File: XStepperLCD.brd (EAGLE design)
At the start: 12.4 x 41.9 mm, 7 parts, among them U1 Attiny85

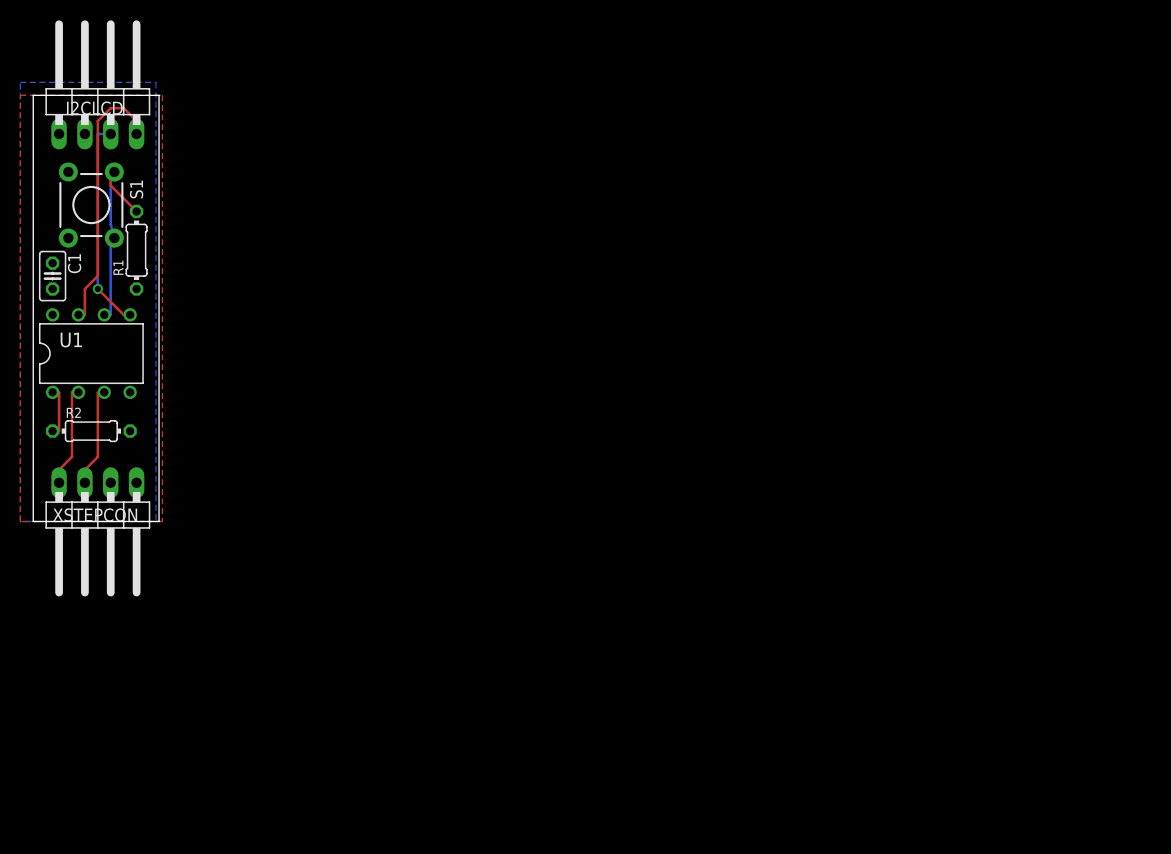
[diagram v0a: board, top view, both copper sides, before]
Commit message: First konzept for XLCD with 328p
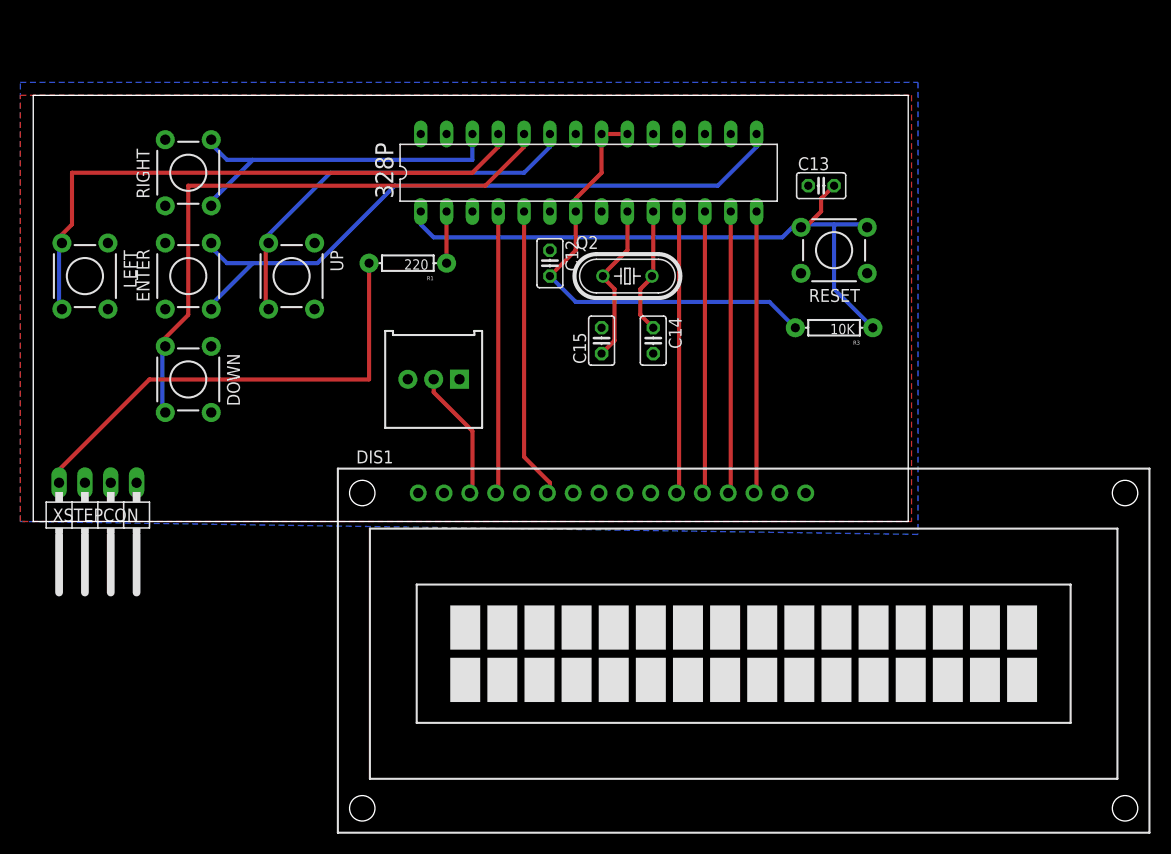
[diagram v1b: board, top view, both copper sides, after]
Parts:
- removed C1: 100nF, rcl:C025-025X050
- removed I2CLCD: i2c, pinhead:1X04/90
- removed S1: Control, SparkFun-Electromechanical:TACTILE-PTH
- removed U1: Attiny85, _hhn_attiny25_45_85:PDIP08_300MIL
- added 328P: CONTROLLER, Bibsatmel:DIL28-3
- added C12, C13: 0.1uF, resistor:C025-025X050
- added C14, C15: 18pF, resistor:C025-025X050
- added DIS1: TUXGR_16X2_R2, display-lcd:TUXGR_16X2_R2
- added DOWN, ENTER, LEFT, RIGHT, UP: (no value), SparkFun:TACTILE-PTH
- added Q2: 16 MHZ, crystal:HC49/S
- added R3: 10K, SparkFun-Resistors:AXIAL-0.3
- added RESET: RESET, SparkFun:TACTILE-PTH
- R1: value 10k -> 220; device resistor:0204/7 -> SparkFun-Resistors:AXIAL-0.3
- R2: value 10k -> 10K; device resistor:0204/7 -> SparkFun-Electromechanical:3386U
- moved R2 34.0 mm to (39.4, 14.0), turned to 180 degrees
- moved R1 26.7 mm to (36.8, 25.4), turned to 180 degrees
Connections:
- removed net CTRL: R1.2, S1.1, S1.2, U1.6
- removed net SCL: I2CLCD.4, U1.7
- removed net SDA: I2CLCD.3, U1.5
- new net 5V: 328P.20, 328P.21, 328P.7, C12.2, R3.P$2
- new net D4: 328P.11, DIS1.11
- new net D5: 328P.12, DIS1.12
- new net D6: 328P.13, DIS1.13
- new net D7: 328P.14, DIS1.14
- new net DOWN: 328P.24, DOWN.3, DOWN.4
- new net E: 328P.5, DIS1.6
- new net ENTER: 328P.15, ENTER.3, ENTER.4
- new net LEFT: 328P.25, LEFT.3, LEFT.4
- new net N$2: DIS1.3, R2.2
- new net N$33: 328P.9, C15.1, Q2.1
- new net N$34: 328P.10, C14.1, Q2.2
- new net RESET: 328P.1, C13.2, R3.P$1, RESET.3, RESET.4
- new net RIGHT: 328P.26, RIGHT.3, RIGHT.4
- new net RS: 328P.4, DIS1.4
- new net TXD: 328P.3
- new net UP: 328P.23, UP.3, UP.4
- net GND: now also 328P.22, 328P.8, C12.1, C13.1, C14.2, C15.2, DIS1.1, DIS1.5, DOWN.1, DOWN.2, ENTER.1, ENTER.2, LEFT.1, LEFT.2, R2.3, RESET.1, RESET.2, RIGHT.1, RIGHT.2, UP.1, UP.2; no longer C1.2, I2CLCD.1, R1.1, U1.4
- net N$1: now also 328P.2, R1.P$1; no longer R2.1, U1.1
- net RX: now also R1.P$2; no longer U1.2
- net TX: no longer U1.3
- net VCC: now also DIS1.2, R2.1; no longer C1.1, I2CLCD.2, R2.2, S1.3, S1.4, U1.8
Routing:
- net ENTER: track 0.00 -> 66.8 mm
- net RESET: track 0.00 -> 63.7 mm
- net DOWN: track 0.00 -> 59.4 mm
- net LEFT: track 0.00 -> 58.3 mm
- net 5V: track 0.00 -> 44.8 mm
- net UP: track 0.00 -> 40.1 mm
- net RX: track 10.1 -> 46.9 mm
- net RIGHT: track 0.00 -> 35.4 mm
- net E: track 0.00 -> 29.4 mm
- net RS: track 0.00 -> 28.3 mm
- net D7: track 0.00 -> 28.3 mm
- net D6: track 0.00 -> 28.3 mm
- net D5: track 0.00 -> 28.3 mm
- net D4: track 0.00 -> 28.3 mm
- net SCL: track 26.3 -> 0.00 mm
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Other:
- board size 12.4 x 41.9 mm -> 86 x 41.9 mm

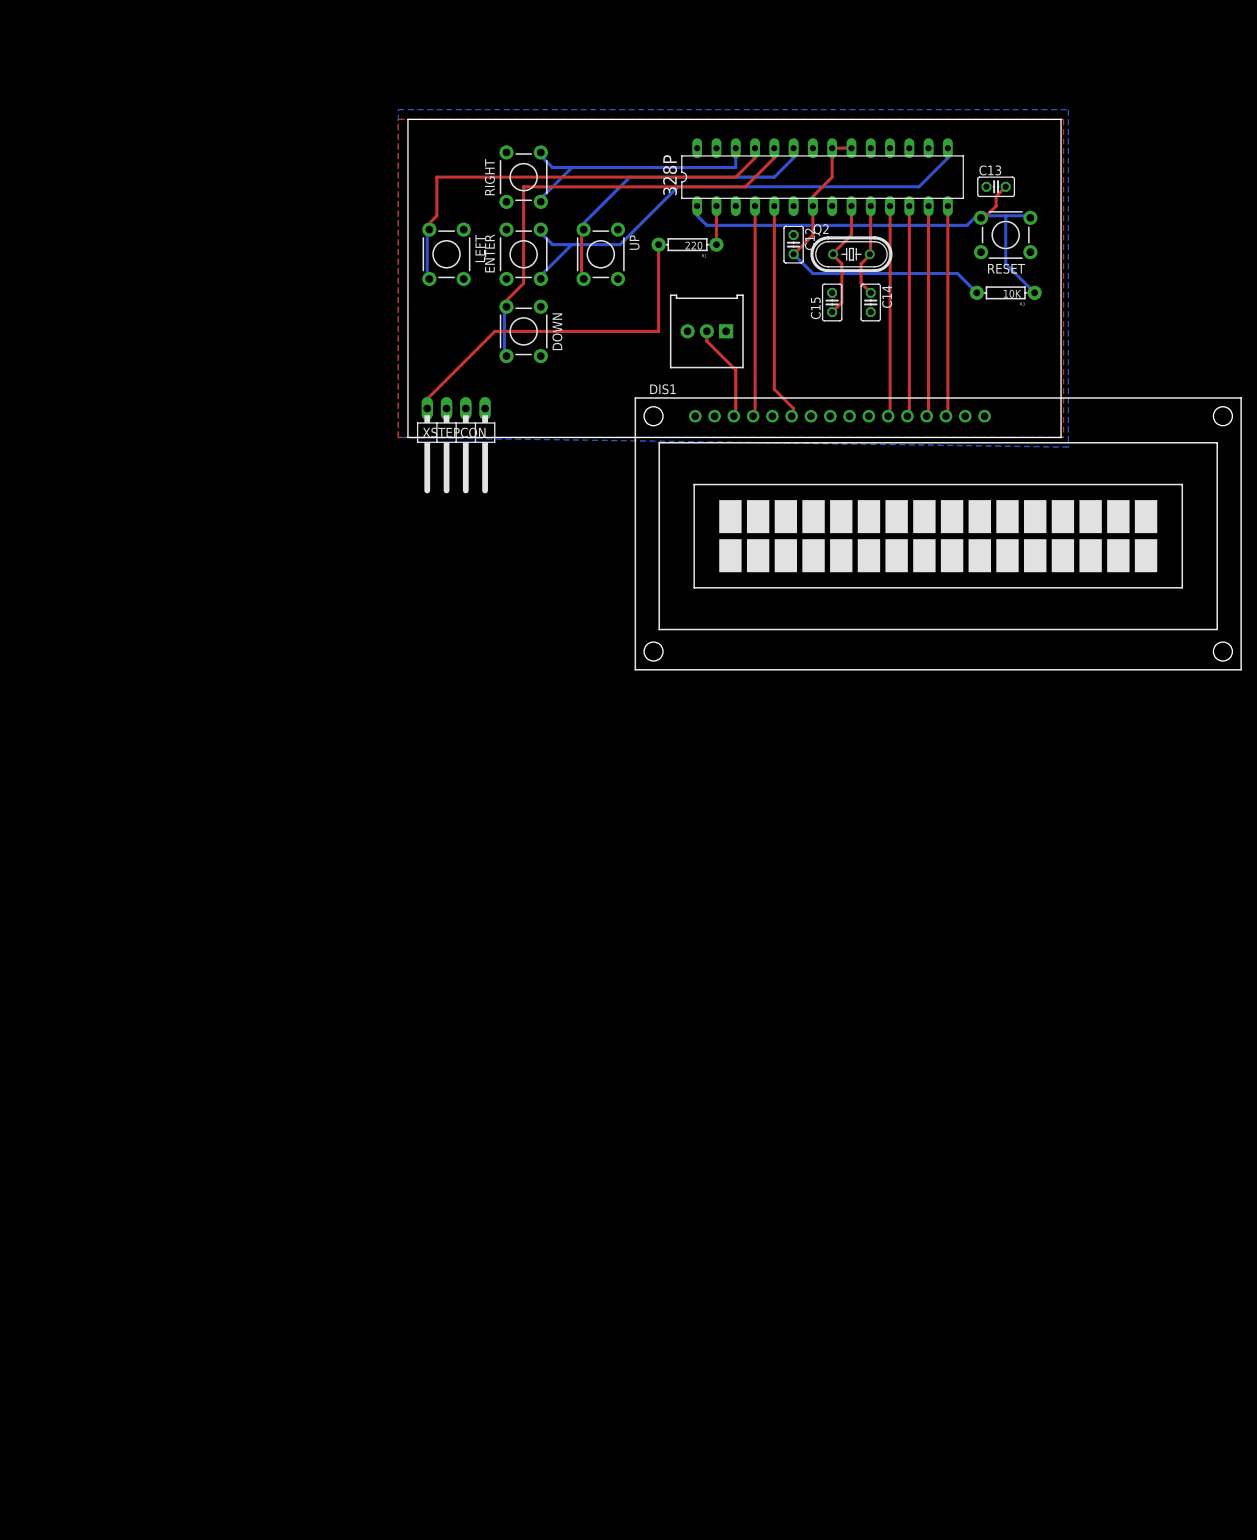
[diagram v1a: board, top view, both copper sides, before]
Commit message: add conn header for buttons
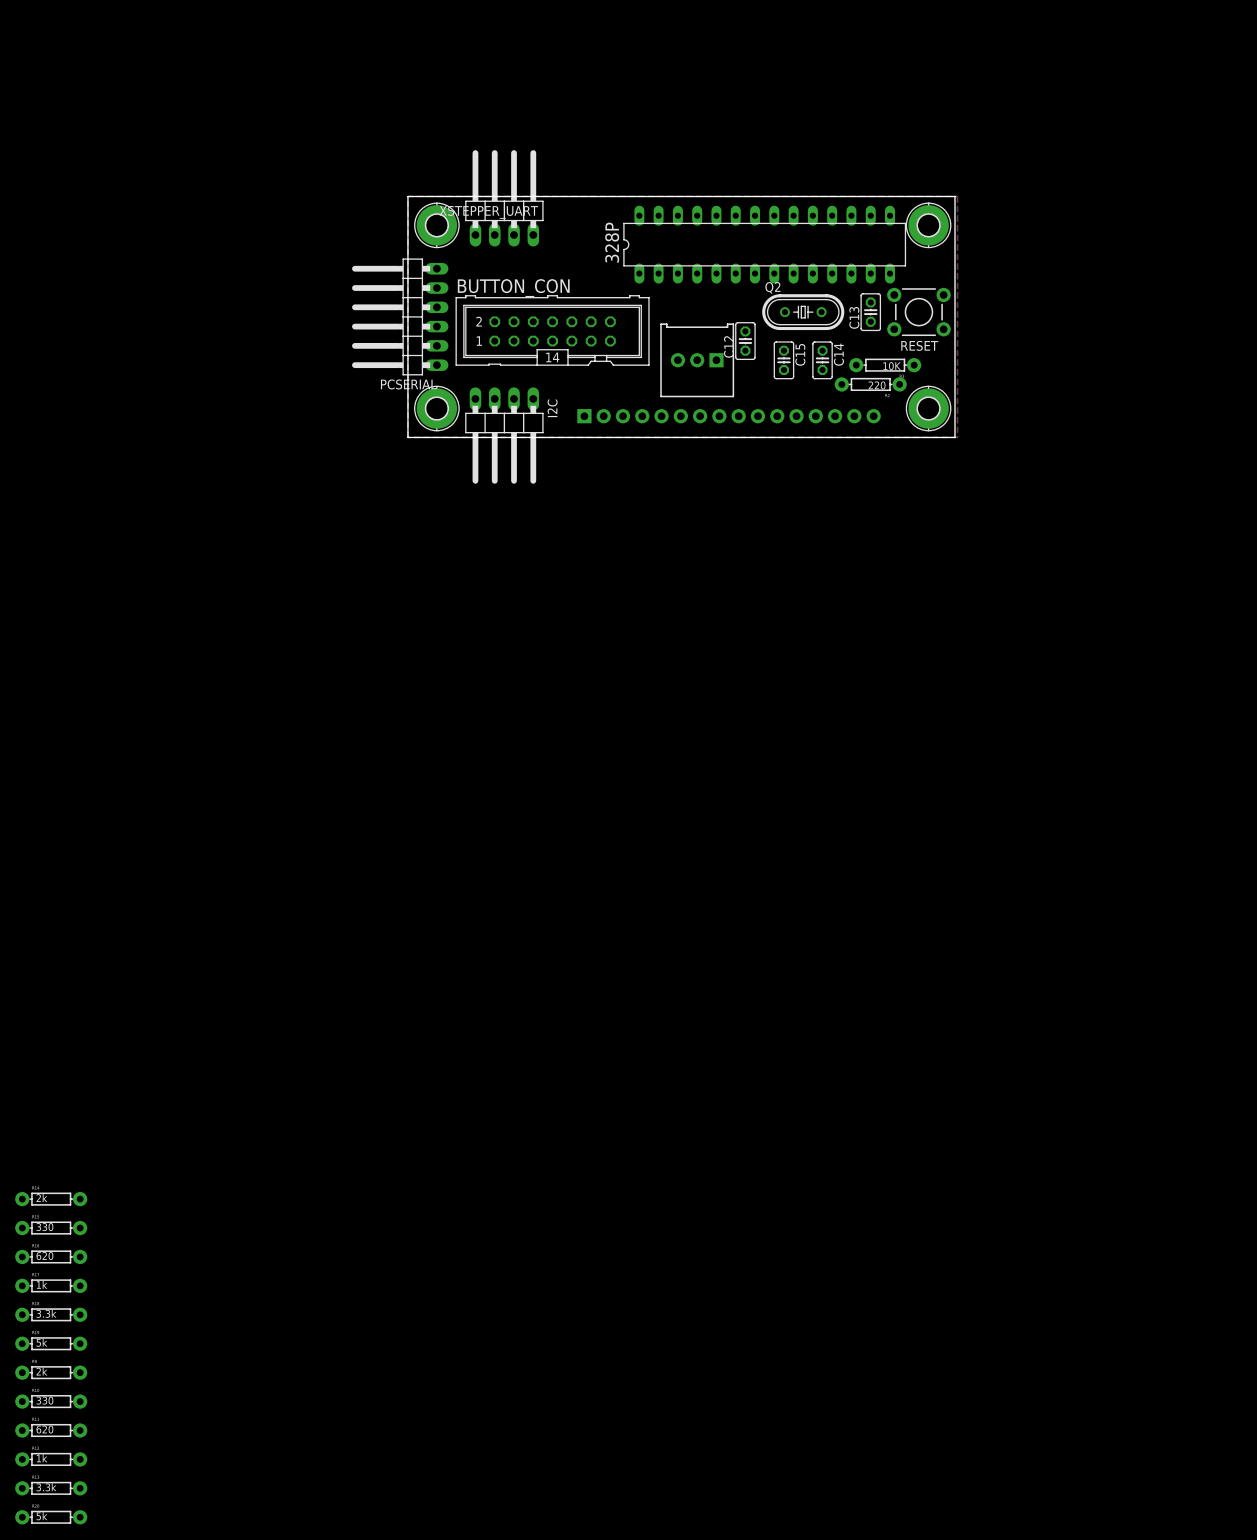
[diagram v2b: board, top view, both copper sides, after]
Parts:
- removed DIS1: TUXGR_16X2_R2, display-lcd:TUXGR_16X2_R2
- removed DOWN, ENTER, LEFT, RIGHT, UP: (no value), SparkFun:TACTILE-PTH
- removed XSTEPCON: serial, pinhead:1X04/90
- added BUTTON_CON: (no value), con-ml:ML14
- added H5, H6, H7, H8: MOUNT-PAD-ROUND2.8, holes:2,8-PAD
- added I2C: i2c, pinhead:1X04/90
- added PCSERIAL: serial, pinhead:1X06/90
- added R10, R15: 330, SparkFun-Resistors:AXIAL-0.3
- added R11, R16: 620, SparkFun-Resistors:AXIAL-0.3
- added R12, R17: 1k, SparkFun-Resistors:AXIAL-0.3
- added R13, R18: 3.3k, SparkFun-Resistors:AXIAL-0.3
- added R14, R9: 2k, SparkFun-Resistors:AXIAL-0.3
- added R19, R20: 5k, SparkFun-Resistors:AXIAL-0.3
- added U1: LCD-16X2NOHOLES, SparkFun-Displays:LCD-16X2_NOHOLES
- added XSTEPPER_UART: serial, pinhead:1X04/90
- R1: value 220 -> 10K; device SparkFun-Resistors:AXIAL-0.3 -> SparkFun-Electromechanical:3386U
- R2: value 10K -> 220; device SparkFun-Electromechanical:3386U -> SparkFun-Resistors:AXIAL-0.3
- moved C13 23.3 mm to (61.0, 16.5), turned to 90 degrees
- moved R2 22.7 mm to (61.0, 6.99)
- moved R3 18.5 mm to (62.9, 9.53)
- moved R1 15.3 mm to (38.1, 10.2)
- moved RESET 15.3 mm to (67.3, 16.5)
- moved C12 14.2 mm to (44.5, 12.7), turned to 90 degrees
- moved 328P 11.7 mm to (47.0, 25.4)
- moved C14 9.92 mm to (54.6, 10.2)
- moved C15 9.92 mm to (49.5, 10.2), turned to 270 degrees
- moved Q2 9.92 mm to (52.1, 16.5)
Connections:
- removed net DOWN: 328P.24, DOWN.3, DOWN.4
- removed net ENTER: 328P.15, ENTER.3, ENTER.4
- removed net LEFT: 328P.25, LEFT.3, LEFT.4
- removed net RIGHT: 328P.26, RIGHT.3, RIGHT.4
- removed net TXD: 328P.3
- removed net UP: 328P.23, UP.3, UP.4
- new net BUTTONS_A: 328P.23, BUTTON_CON.13, R10.P$1, R11.P$1, R12.P$1, R13.P$1, R20.P$1, R9.P$1
- new net BUTTONS_B: 328P.24, BUTTON_CON.14, R14.P$1, R15.P$2, R16.P$2, R17.P$2, R18.P$2, R19.P$2
- new net N$11: BUTTON_CON.12, R15.P$1
- new net N$12: BUTTON_CON.10, R16.P$1
- new net N$13: BUTTON_CON.8, R17.P$1
- new net N$14: BUTTON_CON.6, R18.P$1
- new net N$15: BUTTON_CON.4, R19.P$1
- new net N$16: BUTTON_CON.3, R20.P$2
- new net N$3: BUTTON_CON.11, R10.P$2
- new net N$4: BUTTON_CON.9, R11.P$2
- new net N$5: BUTTON_CON.7, R12.P$2
- new net N$6: BUTTON_CON.5, R13.P$2
- new net SCL: 328P.28, I2C.3
- new net SDA: 328P.27, I2C.2
- new net USB_5V: PCSERIAL.3
- new net USB_RXD: 328P.16, PCSERIAL.5
- new net USB_TXD: 328P.15, PCSERIAL.4
- net D4: now also U1.11; no longer 328P.11, DIS1.11
- net D5: now also 328P.11, U1.12; no longer 328P.12, DIS1.12
- net D6: now also 328P.12, U1.13; no longer 328P.13, DIS1.13
- net D7: now also 328P.13, U1.14; no longer 328P.14, DIS1.14
- net E: now also U1.6; no longer DIS1.6
- net GND: now also BUTTON_CON.1, BUTTON_CON.2, H5.B2,8, H6.B2,8, H7.B2,8, H8.B2,8, I2C.4, PCSERIAL.1, PCSERIAL.2, R1.3, U1.1, U1.10, U1.16, U1.5, U1.7, U1.8, U1.9, XSTEPPER_UART.2; no longer DIS1.1, DIS1.5, DOWN.1, DOWN.2, ENTER.1, ENTER.2, LEFT.1, LEFT.2, R2.3, RIGHT.1, RIGHT.2, UP.1, UP.2, XSTEPCON.2
- net N$1: now also R1.2, U1.3; no longer 328P.2, R1.P$1
- net N$2: now also R2.P$2, U1.15; no longer DIS1.3, R2.2
- net RS: now also U1.4; no longer DIS1.4
- net RX: now also 328P.3, XSTEPPER_UART.4; no longer R1.P$2, XSTEPCON.4
- net TX: now also 328P.2, XSTEPPER_UART.3; no longer XSTEPCON.3
- net VCC: now also I2C.1, R1.1, R14.P$2, R2.P$1, R9.P$2, U1.2, XSTEPPER_UART.1; no longer DIS1.2, R2.1, XSTEPCON.1
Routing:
- net ENTER: track 66.8 -> 0.00 mm
- net RESET: track 63.7 -> 0.00 mm
- net DOWN: track 59.4 -> 0.00 mm
- net LEFT: track 58.3 -> 0.00 mm
- net RX: track 46.9 -> 0.00 mm
- net 5V: track 44.8 -> 0.00 mm
- net UP: track 40.1 -> 0.00 mm
- net RIGHT: track 35.4 -> 0.00 mm
- net E: track 29.4 -> 0.00 mm
- net RS: track 28.3 -> 0.00 mm
- net D7: track 28.3 -> 0.00 mm
- net D6: track 28.3 -> 0.00 mm
- net D5: track 28.3 -> 0.00 mm
- net D4: track 28.3 -> 0.00 mm
- net N$33: track 16.2 -> 0.00 mm
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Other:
- board size 86 x 41.9 mm -> 72.1 x 31.7 mm
- board text removed: "Frank (xpix) Herrmann 2013"
- board text removed: "XStepper LCD 0.1"
